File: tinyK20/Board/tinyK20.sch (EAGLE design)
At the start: 76 parts, among them IC1 MK20DX128VFT5, IC2 TC1262, IC3 74AHC1G125GW, P1 SOLDERPAD, P10 SOLDERPAD, P11 SOLDERPAD, P12 SOLDERPAD, P13 SOLDERPAD, P14 SOLDERPAD, P15 SOLDERPAD, P16 SOLDERPAD, P17 SOLDERPAD, P18 SOLDERPAD, P19 SOLDERPAD, P2 SOLDERPAD, P20 SOLDERPAD, P21 SOLDERPAD, P22 SOLDERPAD, P23 SOLDERPAD, P25 SOLDERPAD, P26 SOLDERPAD, P27 SOLDERPAD, P28 SOLDERPAD, P29 SOLDERPAD, P3 SOLDERPAD, P30 SOLDERPAD, P31 SOLDERPAD, P32 SOLDERPAD, P33 SOLDERPAD, P34 SOLDERPAD, P35 SOLDERPAD, P36 SOLDERPAD, P4 SOLDERPAD, P40 SOLDERPAD, P41 SOLDERPAD, P5 SOLDERPAD, P6 SOLDERPAD, P7 SOLDERPAD, P8 SOLDERPAD, P9 SOLDERPAD, X2 MINI-USB-SHIELDHIROSE-UX60SC-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, X3 STIFTLEISTE_2X5_1.27-SMD, X4 MOLEX-MICRO-SD, X8 STIFTLEISTE_2X5_1.27-SMD, Y1 AB38T, Y2 8MHz

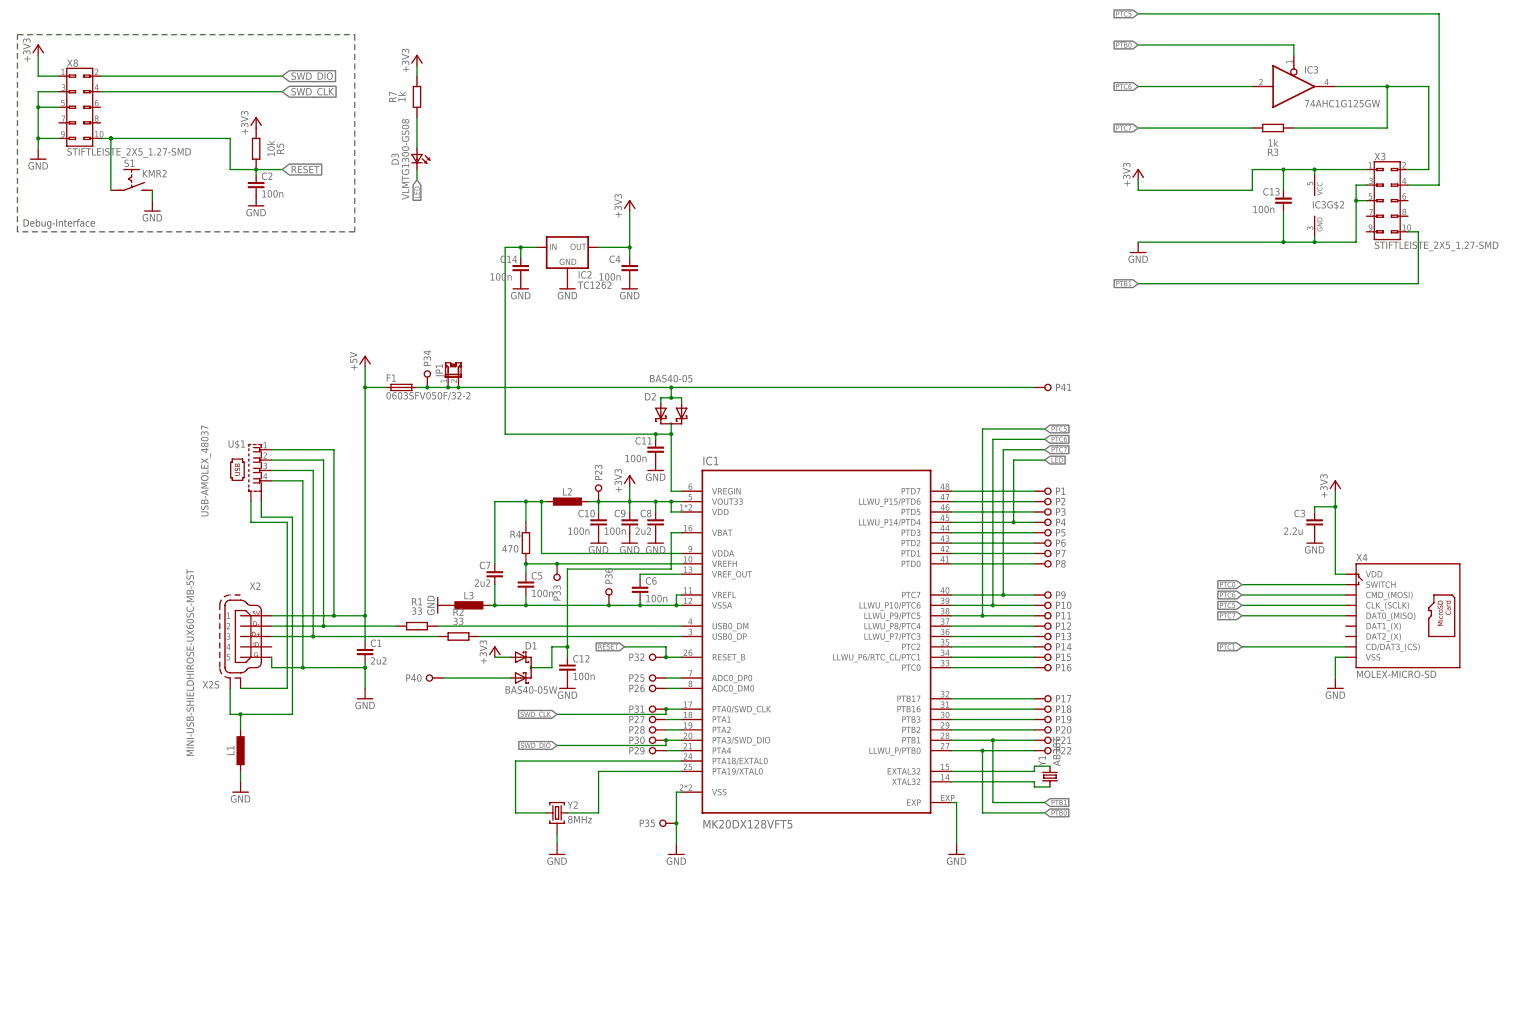
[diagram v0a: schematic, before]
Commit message: new version with UART to SWD connections
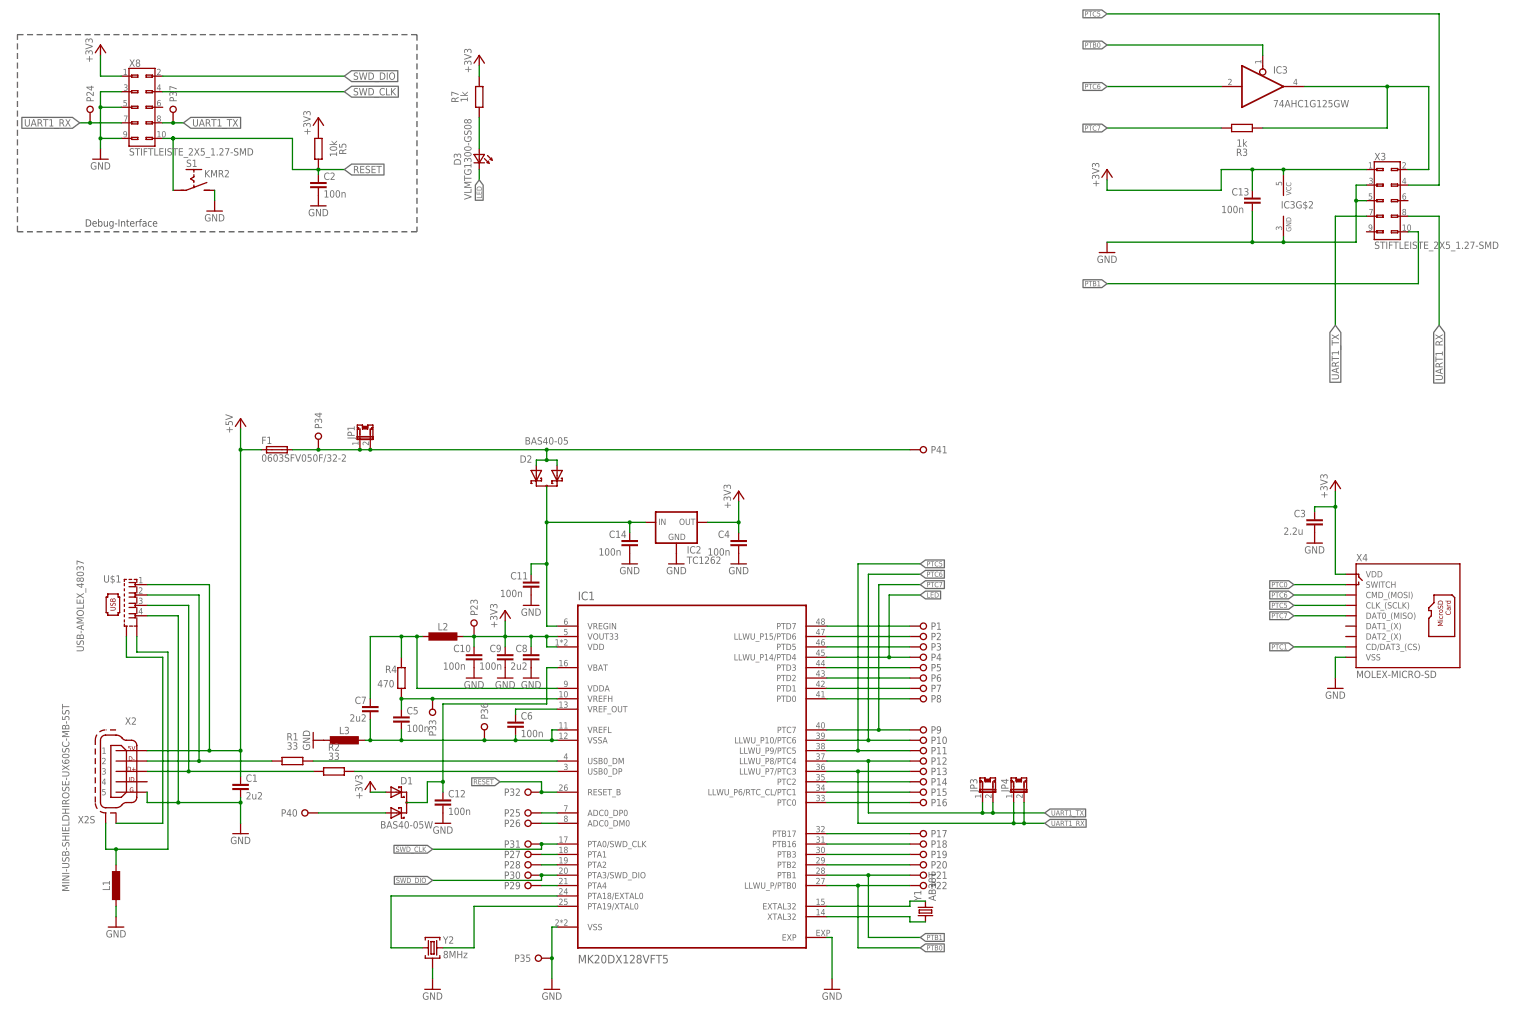
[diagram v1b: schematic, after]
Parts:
- added JP3, JP4: JP1-SMD-1.2X1.8, misc:JP1-SMD-1.2X1.8
- added P24, P37: SOLDERPAD, connectors:SOLDERPAD
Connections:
- removed net N$27: IC1.LLWU_P8/PTC4, P12.PAD
- removed net N$28: IC1.LLWU_P7/PTC3, P13.PAD
- new net UART1_RX: IC1.LLWU_P7/PTC3, JP4A.1, JP4A.2, P13.PAD, P24.PAD, X3.8, X8.7
- new net UART1_TX: IC1.LLWU_P8/PTC4, JP3A.1, JP3A.2, P12.PAD, P37.PAD, X3.7, X8.8
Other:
- moved on the sheet: C1, C10, C11, C12, C13, C14, C2, C4, C5, C6, C7, C8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
